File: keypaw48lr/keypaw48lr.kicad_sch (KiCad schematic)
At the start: 103 parts, among them J1 Conn_01x02, J2 Conn_01x02, J3 Conn_01x02, J4 Conn_01x02, J5 Conn_01x02, J6 JD9613_OLED_FPC_Conn_01x10, J7 JD9613_OLED_FPC_Conn_01x10, SW1 SW_SPDT, SW2 RotaryEncoder, U1 nice_nano, U2 PAW3395, U3 TLV70019_SOT23-5, U4 TPS22917DBV

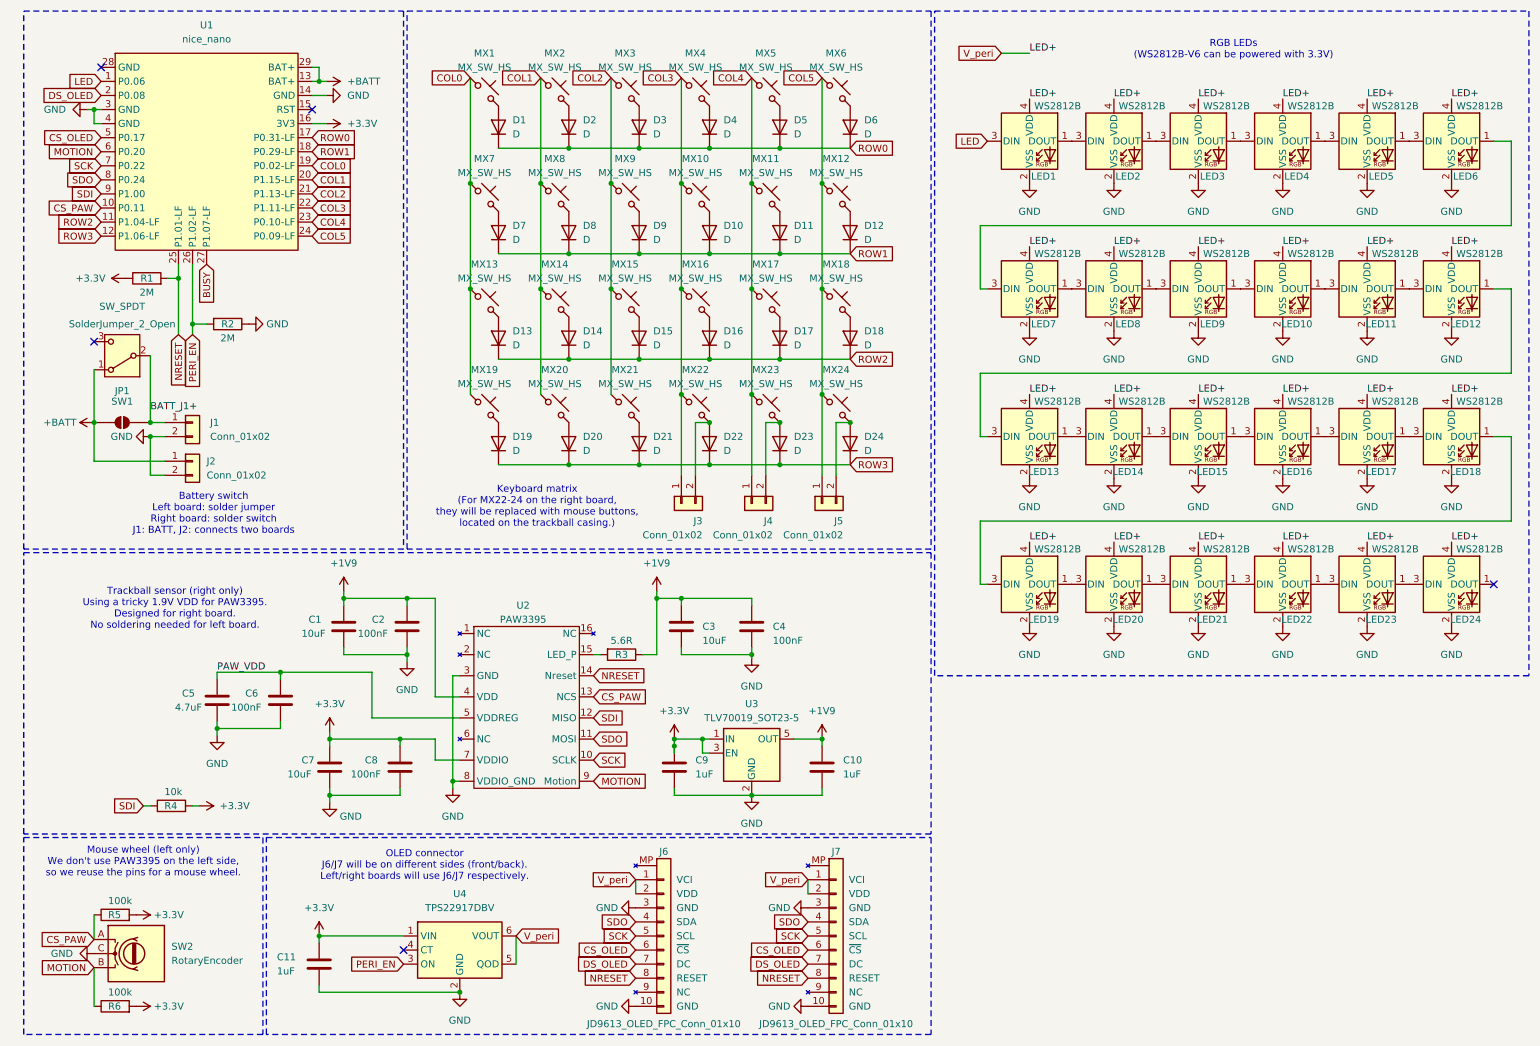
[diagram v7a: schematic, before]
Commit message: feat: add some more led lights
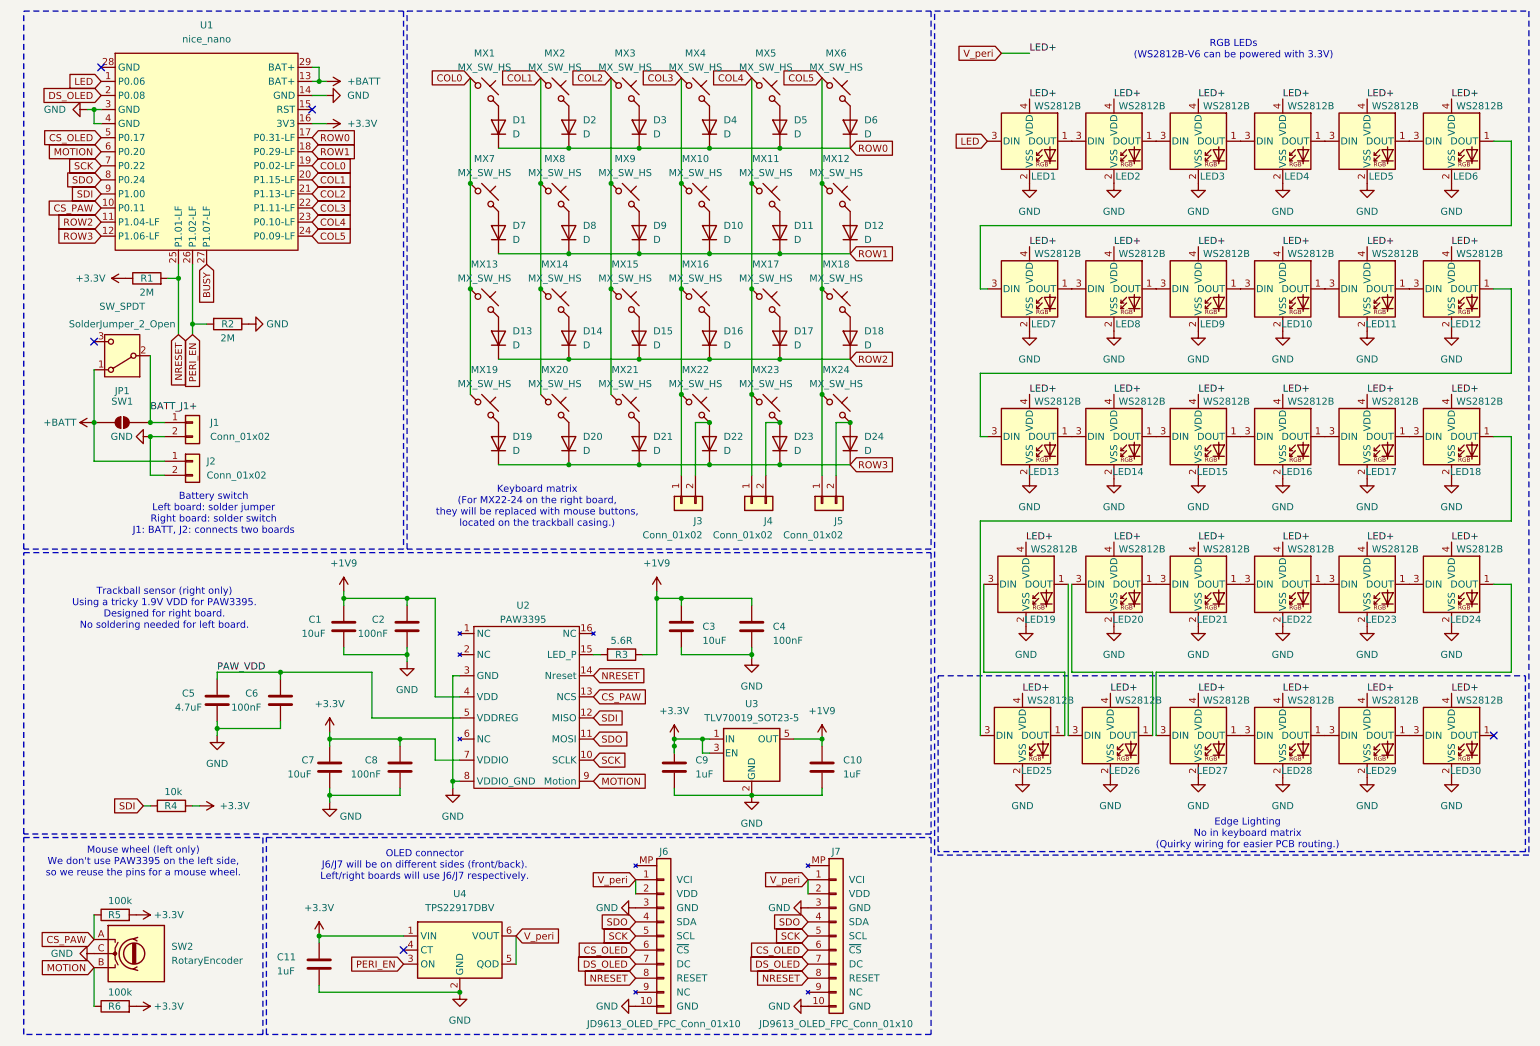
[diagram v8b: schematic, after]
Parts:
- added LED25, LED26, LED27, LED28, LED29, LED30: WS2812B, WS2812B_2020_V6:LED_WS2812B-2020_backmount_rev, symbol WS2812B_2020_V6:WS2812B-2020-V6
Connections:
- net GND: now also LED25.2 (VSS), LED26.2 (VSS), LED27.2 (VSS), LED28.2 (VSS), LED29.2 (VSS), LED30.2 (VSS)
- net V_peri: now also LED25.4 (VDD), LED26.4 (VDD), LED27.4 (VDD), LED28.4 (VDD), LED29.4 (VDD), LED30.4 (VDD)
- net at LED18.1 (DOUT): now also LED25.3 (DIN); no longer LED19.3 (DIN)
- net at LED19.1 (DOUT): now also LED26.3 (DIN); no longer LED20.3 (DIN)
- net at LED24.1 (DOUT): now also LED27.3 (DIN)
- new net: LED19.3 (DIN), LED25.1 (DOUT)
- new net: LED20.3 (DIN), LED26.1 (DOUT)
- new net: LED29.1 (DOUT), LED30.3 (DIN)
- new net: LED28.1 (DOUT), LED29.3 (DIN)
- new net: LED27.1 (DOUT), LED28.3 (DIN)
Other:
- note added: "Edge Lighting No in keyboard matrix (Quirky wiring for easier PCB routing.)"
- company: (none) -> Kana
- title: (none) -> Keypaw48 Schematic (Left & Right Board)
- moved on the sheet: LED19
